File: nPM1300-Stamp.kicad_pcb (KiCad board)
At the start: 4 copper layers, 18 x 18 mm, 16 parts, among them J1 Conn_01x08, J2 Conn_01x08, J3 Conn_01x08, J4 Conn_01x08, U1 nPM1300-QEXX

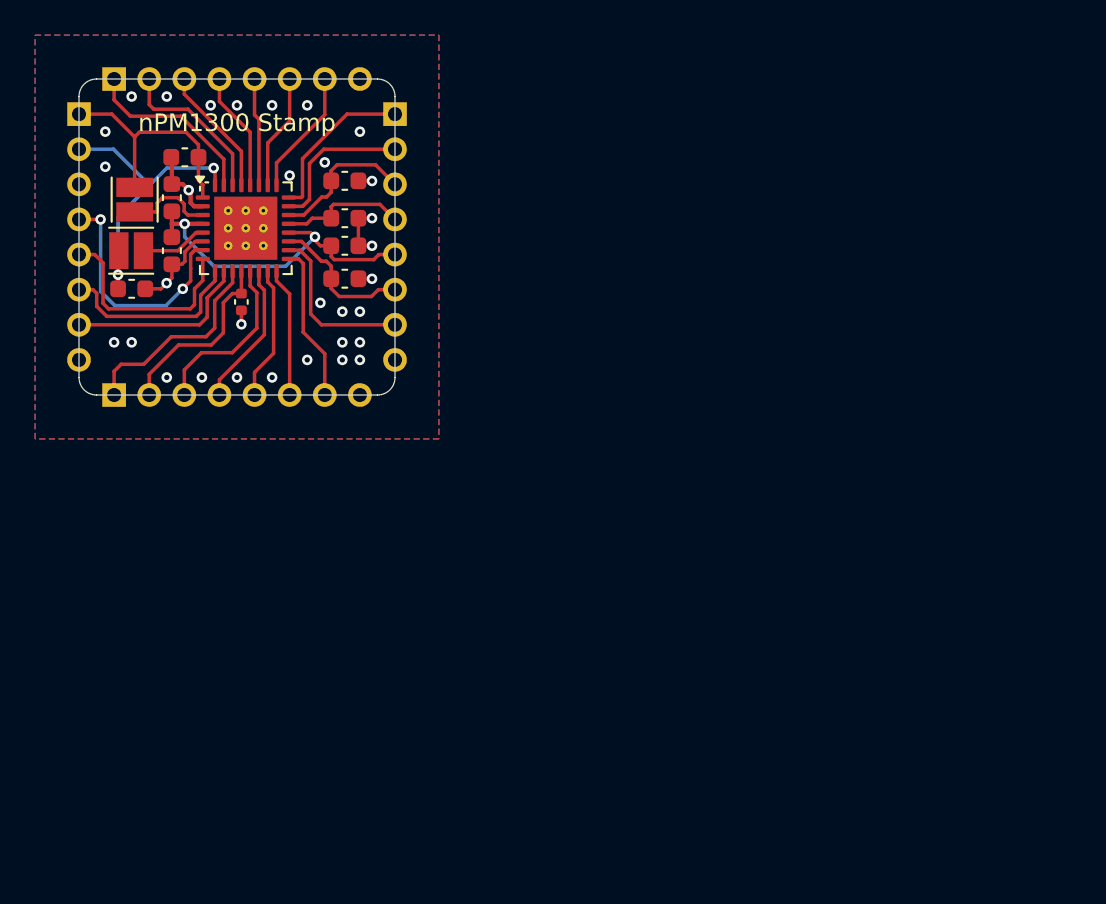
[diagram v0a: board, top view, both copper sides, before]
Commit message: Added nPM1300 library
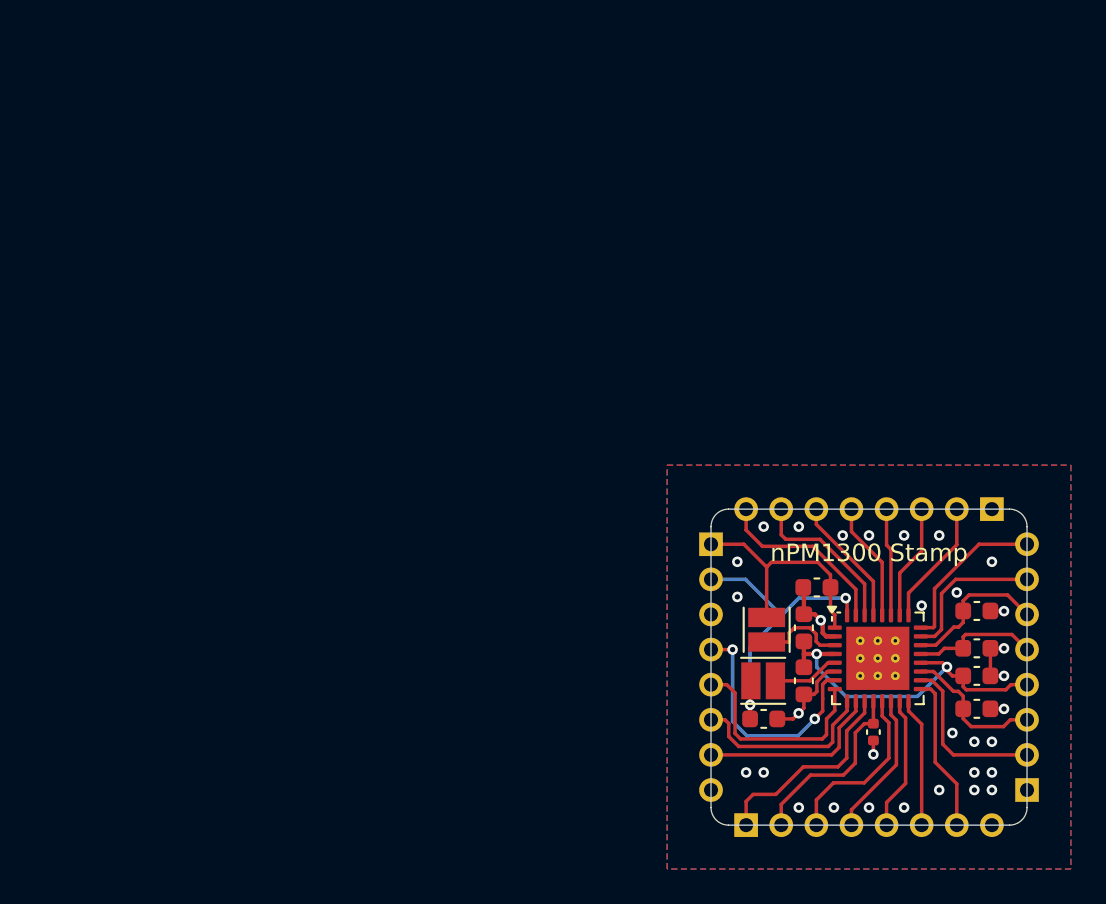
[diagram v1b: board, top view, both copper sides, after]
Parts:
- moved J4 55.7 mm to (157.0, 91.0), turned to -90 degrees
- moved J3 52.7 mm to (159.0, 107.0), turned to 180 degrees
- moved C1 43.5 mm to (150.2, 103.7)
- moved C7 43.5 mm to (147.0, 95.5)
- moved C8 43.5 mm to (144.0, 103.0)
- moved J1 43.5 mm to (141.0, 93.0)
- moved J2 43.5 mm to (143.0, 109.0)
- moved L2 43.5 mm to (144.0, 100.8)
- moved U1 43.5 mm to (150.5, 99.5)
- moved C13 43.5 mm to (156.1, 102.4)
- moved C2 43.5 mm to (146.3, 100.8)
- moved C3 43.5 mm to (146.3, 97.8)
- moved C4 43.5 mm to (156.1, 100.5)
- moved C5 43.5 mm to (156.1, 98.9)
- moved C6 43.5 mm to (156.1, 96.8)
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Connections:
- J3 pad 1: /CC2 -> GND
- J3 pad 2: /CC1 -> /NTC
- J3 pad 3: /VBUS_OUT -> /VBAT
- J3 pad 4: /VBUS_IN -> /VSYS
- J3 pad 5: /VSYS -> /VBUS_IN
- J3 pad 6: /VBAT -> /VBUS_OUT
- J3 pad 7: /NTC -> /CC1
- J3 pad 8: GND -> /CC2
- J4 pad 1: /LS2_OUT -> GND
- J4 pad 2: /LS2_IN -> /LED0
- J4 pad 3: /LS1_OUT -> /LED1
- J4 pad 4: /LS1_IN -> /LED2
- J4 pad 5: /LED2 -> /LS1_IN
- J4 pad 6: /LED1 -> /LS1_OUT
- J4 pad 7: /LED0 -> /LS2_IN
- J4 pad 8: GND -> /LS2_OUT

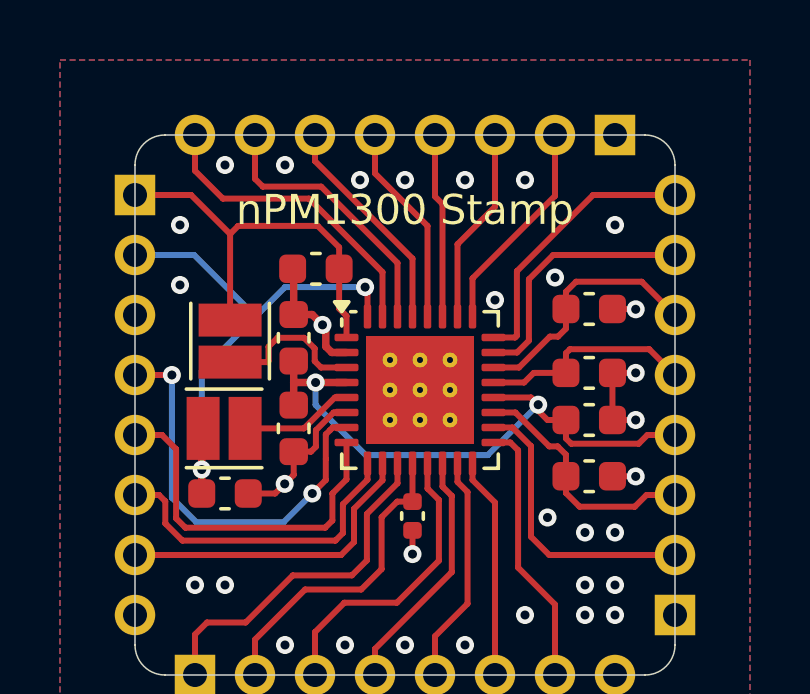
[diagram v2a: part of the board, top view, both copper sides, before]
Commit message: Updated layout to use thicker traces for power delivery
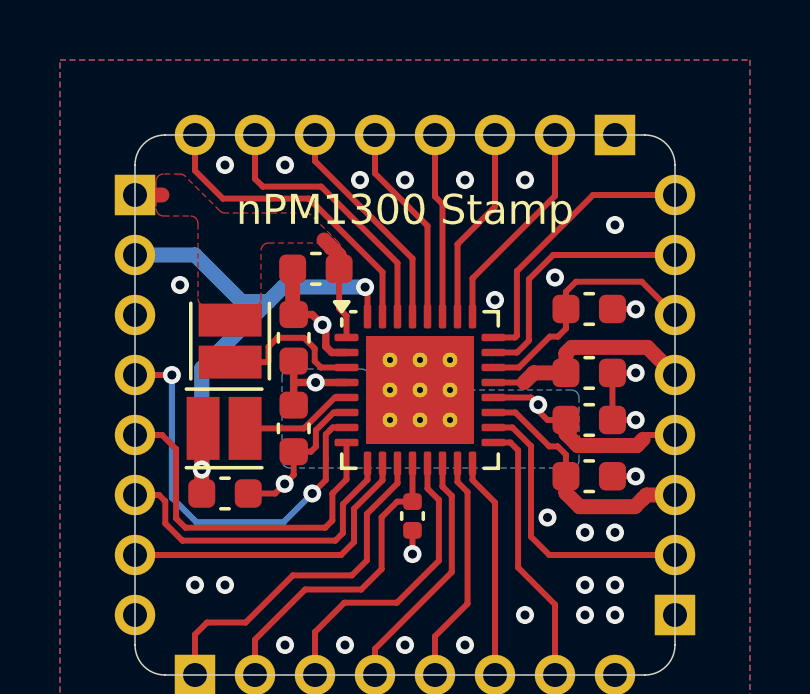
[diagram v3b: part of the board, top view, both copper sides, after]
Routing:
- net /VSYS: track 20.1 -> 10.5 mm
- net /VOUT1: track 13.7 -> 4.46 mm
- net GND: vias 32 -> 31
- added copper zone on F.Cu, net /VOUT1
- added copper zone on B.Cu, net /VSYS

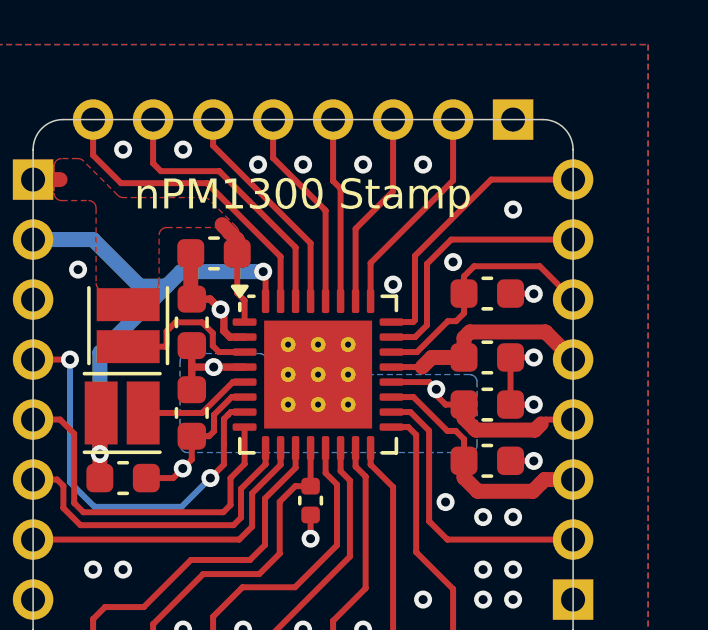
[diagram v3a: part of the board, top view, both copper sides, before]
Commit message: Updated LCSC part number for 2.2uF cap
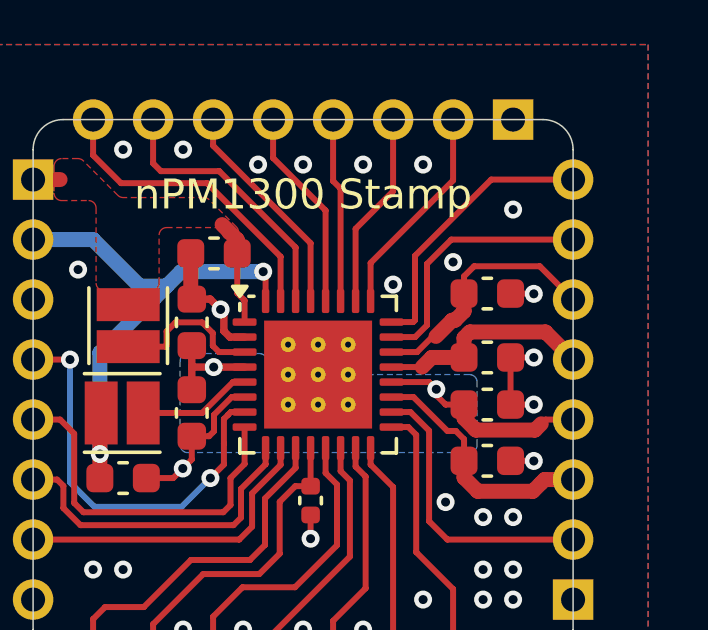
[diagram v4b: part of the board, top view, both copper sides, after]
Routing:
- net /VBUS_OUT: track 8.41 -> 10.3 mm
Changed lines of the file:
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@@
 		(sheetname "Root")
 		(sheetfile "nPM1300-Stamp.kicad_sch")
-		(attr through_hole exclude_from_pos_files exclude_from_bom dnp)
+		(attr through_hole exclude_from_pos_files dnp)
 		(fp_line
 			(start -1.5 15.5)
@@
 			)
 		)
-		(property "LCSC" "C50254"
+		(property "LCSC" "C23630"
 			(at 0 0 0)
 			(unlocked yes)
@@
 		(sheetname "Root")
 		(sheetfile "nPM1300-Stamp.kicad_sch")
-		(attr through_hole exclude_from_pos_files exclude_from_bom dnp)
+		(attr through_hole exclude_from_pos_files dnp)
 		(fp_line
 			(start 1.5 15.5)
@@
 		(sheetname "Root")
 		(sheetfile "nPM1300-Stamp.kicad_sch")
-		(attr through_hole exclude_from_pos_files exclude_from_bom dnp)
+		(attr through_hole exclude_from_pos_files dnp)
 		(fp_line
 			(start -1.5 -1.5)
@@
 		(sheetname "Root")
 		(sheetfile "nPM1300-Stamp.kicad_sch")
-		(attr through_hole exclude_from_pos_files exclude_from_bom dnp)
+		(attr through_hole exclude_from_pos_files dnp)
 		(fp_line
 			(start 1.5 -1.5)
@@
 	)
 	(segment
+		(start 155.068059 97.688058)
+		(end 154.96938 97.688058)
+		(width 0.5)
+		(layer "F.Cu")
+		(net 3)
+	)
+	(segment
 		(start 155.365 97.455)
 		(end 155.365 96.8)
@@
 	)
 	(segment
+		(start 155.365 97.391117)
+		(end 155.068059 97.688058)
+		(width 0.5)
+		(layer "F.Cu")
+		(net 3)
+	)
+	(segment
 		(start 155.365 96.225)
 		(end 155.7 95.89)
@@
 	)
 	(segment
+		(start 155.365 96.8)
+		(end 155.365 97.391117)
+		(width 0.5)
+		(layer "F.Cu")
+		(net 3)
+	)
+	(segment
 		(start 157.89 95.89)
 		(end 159 97)
@@
 		(layer "F.Cu")
 		(net 3)
+	)
+	(segment
+		(start 154.96938 97.688058)
+		(end 154.428719 98.228719)
+		(width 0.5)
+		(layer "F.Cu")
+		(net 3)
